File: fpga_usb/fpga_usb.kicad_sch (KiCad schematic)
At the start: 1 part

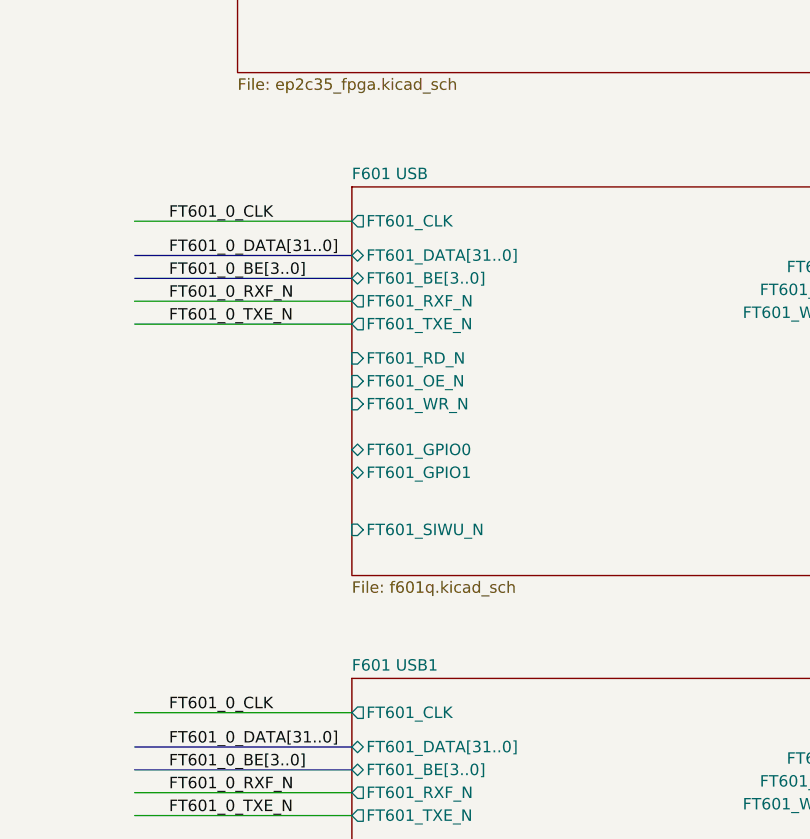
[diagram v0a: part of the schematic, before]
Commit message: Import USB3 switch. Narrow Netclass.
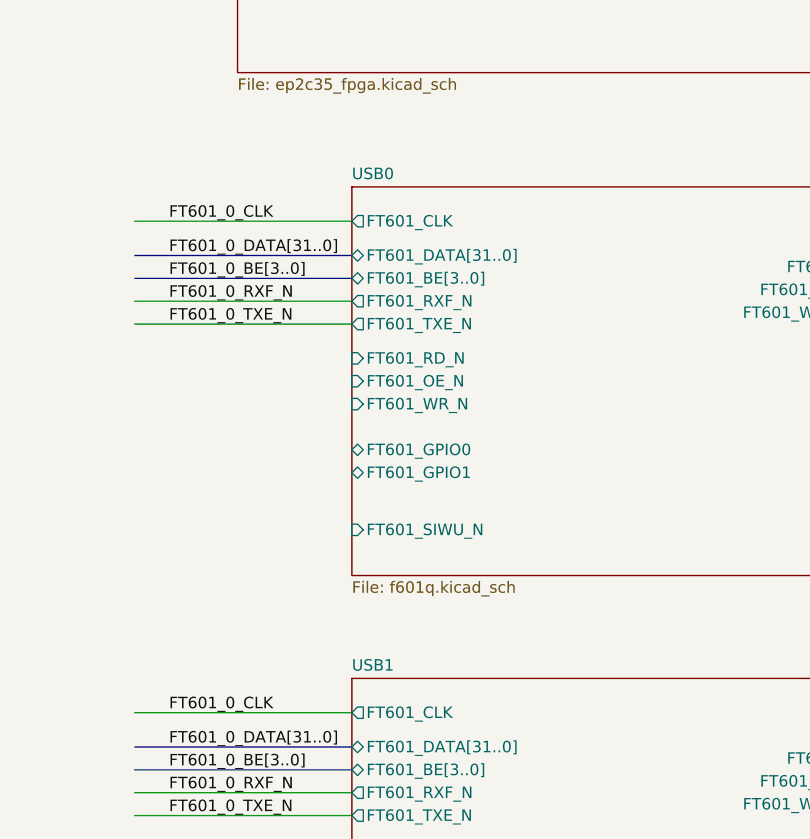
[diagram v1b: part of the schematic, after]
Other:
- sheet F601 USB renamed USB0
- sheet F601 USB1 renamed USB1
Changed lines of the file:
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@@
 			(color 0 0 0 0.0000)
 		)
-		(property "Sheetname" "F601 USB1"
+		(property "Sheetname" "USB1"
 			(at 222.25 188.5184 0)
 			(effects
@@
 			(color 0 0 0 0.0000)
 		)
-		(property "Sheetname" "F601 USB"
+		(property "Sheetname" "USB0"
 			(at 222.25 133.9084 0)
 			(effects

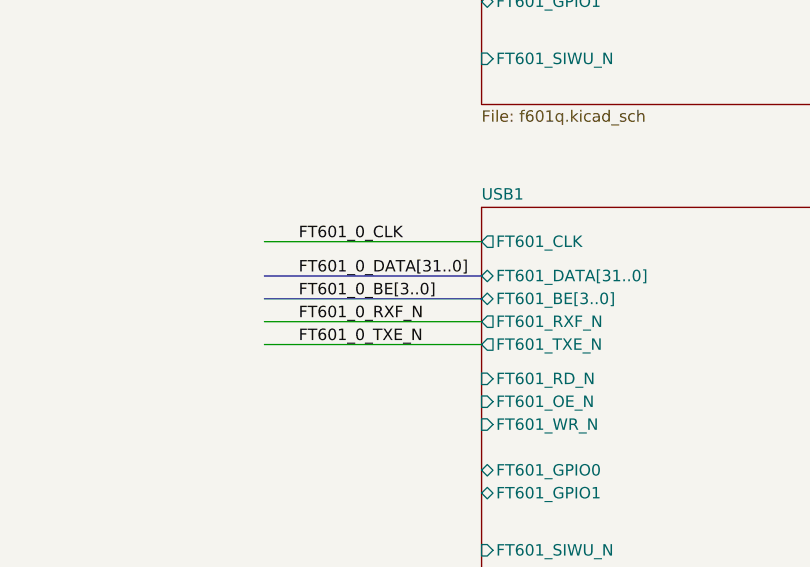
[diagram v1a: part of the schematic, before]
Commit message: First placement trial of USB0.
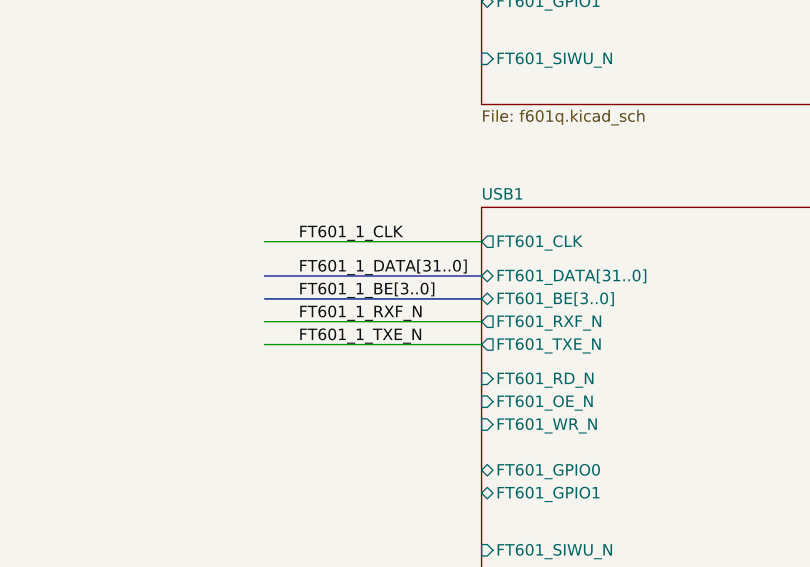
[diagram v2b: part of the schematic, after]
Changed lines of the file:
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@@
 		)
 	)
-	(label "FT601_0_DATA[31..0]"
+	(label "FT601_1_DATA[31..0]"
 		(at 201.93 196.85 0)
 		(effects
@@
 		)
 	)
-	(label "FT601_0_CLK"
+	(label "FT601_1_CLK"
 		(at 201.93 193.04 0)
 		(effects
@@
 		)
 	)
-	(label "FT601_0_TXE_N"
+	(label "FT601_1_TXE_N"
 		(at 201.93 204.47 0)
 		(effects
@@
 		)
 	)
-	(label "FT601_0_BE[3..0]"
+	(label "FT601_1_BE[3..0]"
 		(at 201.93 199.39 0)
 		(effects
@@
 		)
 	)
-	(label "FT601_0_RXF_N"
+	(label "FT601_1_RXF_N"
 		(at 201.93 201.93 0)
 		(effects
